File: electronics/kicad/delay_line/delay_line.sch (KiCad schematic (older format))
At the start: 26 parts, among them J1 TEENSY, J2 TEENSY, J3 DEFLECTION, J6 DEFLECTION, P1 CONN_2, Q1 TSM2N100CHC5G, Q3 BSS84, Q4 ZTX458, U1 DS1023S-50, U2 DS1100Z-500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

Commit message: Progress
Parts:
- removed C4: 0.1 uF, Capacitor_SMD:C_0603_1608Metric, symbol SparkFun-Capacitors:0.1UF-KIT-EZ-50V-20%
- removed C5: 50 pF, Capacitor_SMD:C_1206_3216Metric, symbol SparkFun-Capacitors:0.1UF-KIT-EZ-50V-20%
- removed D2: D_TVS, Diode_SMD:D_SMA, symbol Device:D_TVS
- removed J3, J6: DEFLECTION, Connectors2:1X03_SMD_RA_MALE, symbol w_connectors:HEADER_3
- removed Q1: TSM2N100CHC5G, Package_TO_SOT_SMD:TO-252-3_TabPin2, symbol Transistor_FET:NTR2101P
- removed Q3: BSS84, Package_TO_SOT_SMD:SOT-23, symbol Transistor_FET:BSS84
- removed Q4: ZTX458, Package_TO_SOT_THT:TO-92S_Wide, symbol SparkFun-DiscreteSemi:TRANS_NPN-2N3904
- removed R1: 10k, 0603, symbol SparkFun-Resistors:RESISTOR0603
- removed R2, R4, R5: 400k, 1206, symbol SparkFun-Resistors:RESISTOR1206
- removed VR1: TRIMPOT-PTH-10MM-KNOB-1_2W-10%, TRIMPOT-PTH-3386U, symbol SparkFun-Resistors:TRIMPOT-PTH-10MM-KNOB-1_2W-10%
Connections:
- net labels removed: HV, HV_CENTER, SWEEP, VSWEEP_SLOPE
- wire segments 16 -> 8
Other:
- note removed: "This is here because the rate of charge of coax line might be slow, affecting\nthe linearity of the ramp\n"
- note removed: "coax"
- note removed: "ramp generator based on Baker and Johnson"

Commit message: Coplanar exposure cell working
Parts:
- added C?: 0.1UF-0603-25V-5%, 0603, symbol SparkFun-Capacitors:0.1UF-0603-25V-5%
- added R?: 50 ohm, 0805, symbol SparkFun-Resistors:RESISTOR0805
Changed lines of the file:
@@
 Text GLabel 10250 4900 2    50   Input ~ 0
 COAX
-Wire Wire Line
-	9200 2250 9850 2250
 $Comp
 L conn:CONN_2 P1
@@
 	1    0    0    -1
 $EndComp
+$Comp
+L SparkFun-Capacitors:0.1UF-0603-25V-5% C?
+U 1 1 6016D4E6
+P 10250 2250
+F 0 "C?" V 10484 2300 45  0000 C CNN
+F 1 "0.1UF-0603-25V-5%" V 10400 2300 45  0000 C CNN
+F 2 "0603" H 10250 2500 20  0001 C CNN
+F 3 "" H 10250 2250 50  0001 C CNN
+F 4 "" V 10411 2300 60  0000 C CNN "Field4"
+	1    10250 2250
+	0    -1   -1   0
+$EndComp
+Wire Wire Line
+	9200 2250 10050 2250
+$Comp
+L SparkFun-Resistors:RESISTOR0805 R?
+U 1 1 6016EE58
+P 10350 2450
+F 0 "R?" V 10255 2518 45  0000 L CNN
+F 1 "50 ohm" V 10339 2518 45  0000 L CNN
+F 2 "0805" H 10350 2600 20  0001 C CNN
+F 3 "" H 10350 2450 60  0001 C CNN
+F 4 " " V 10434 2518 60  0000 L CNN "Field4"
+	1    10350 2450
+	0    1    1    0
+$EndComp
+$Comp
+L power:GND #PWR?
+U 1 1 6016FF07
+P 10350 2650
+F 0 "#PWR?" H 10350 2650 30  0001 C CNN
+F 1 "GND" H 10350 2580 30  0001 C CNN
+F 2 "" H 10350 2650 50  0001 C CNN
+F 3 "" H 10350 2650 50  0001 C CNN
+	1    10350 2650
+	1    0    0    -1
+$EndComp

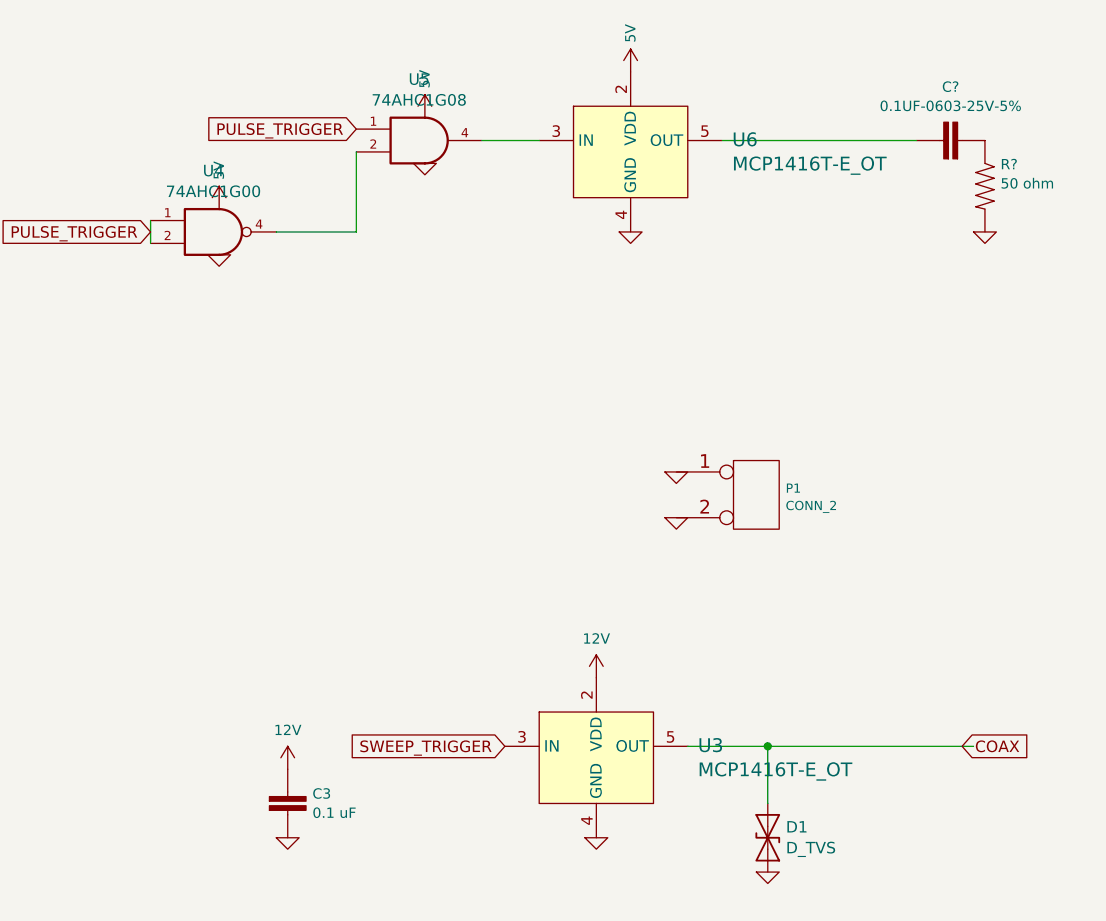
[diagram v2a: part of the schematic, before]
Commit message: Delay line functioning great
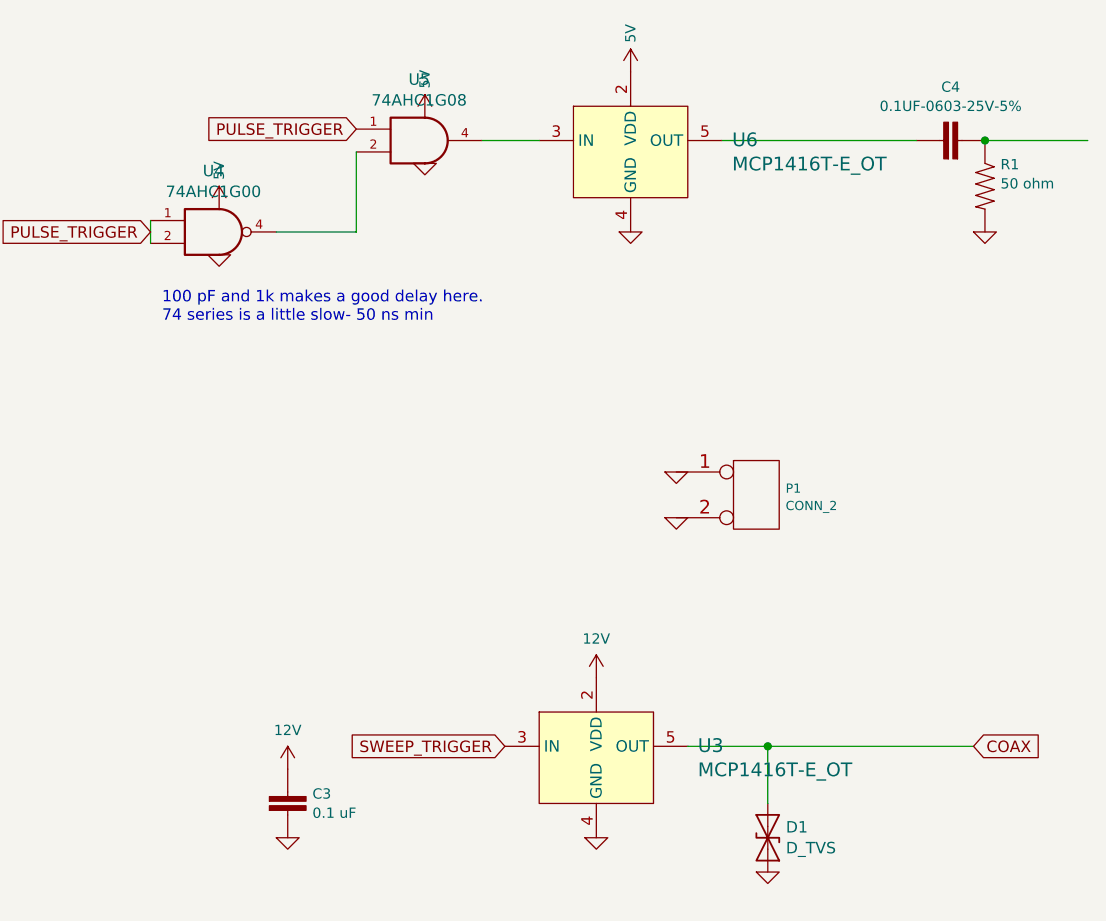
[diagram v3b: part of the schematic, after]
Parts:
- gave numbers to parts that had none: 2
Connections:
- wire segments 8 -> 9
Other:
- note added: "100 pF and 1k makes a good delay here. \n74 series is a little slow- 50 ns min"
